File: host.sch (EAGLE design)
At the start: 106 parts, among them IC1 74LVC1T45GS,132, IC10 74LVC1T45GS,132, IC11 74LVC1T45GS,132, IC2 NCP187AMT120TAG, IC3 LD39200PU33R, IC4 74LVC1T45GS,132, IC5 74LVC1T45GS,132, IC6 74LVC1T45GS,132, IC7 74ALVC164245DGG:11, IC8 74ALVC164245DGG:11, IC9 74LVC1T45GS,132, Y1 DSC6001J

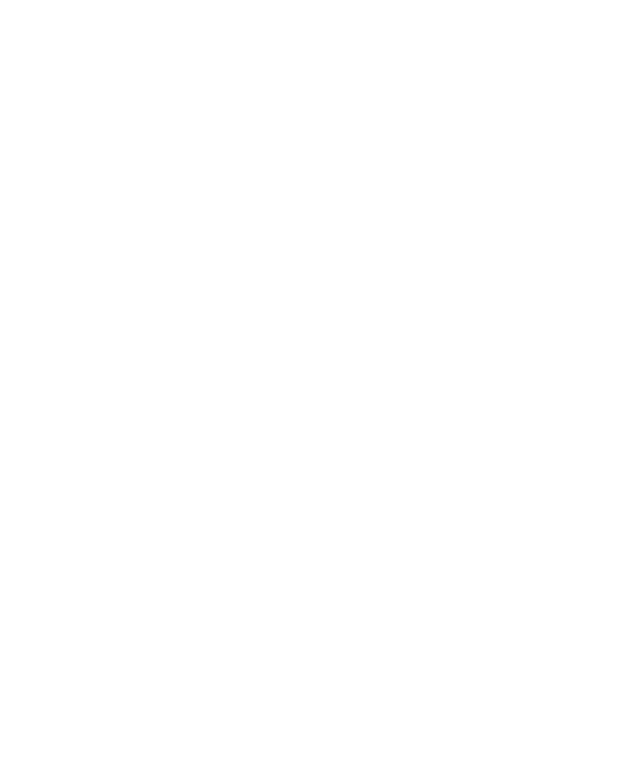
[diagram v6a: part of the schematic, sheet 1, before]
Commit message: Move to micro-HDMI for the interconnect cable
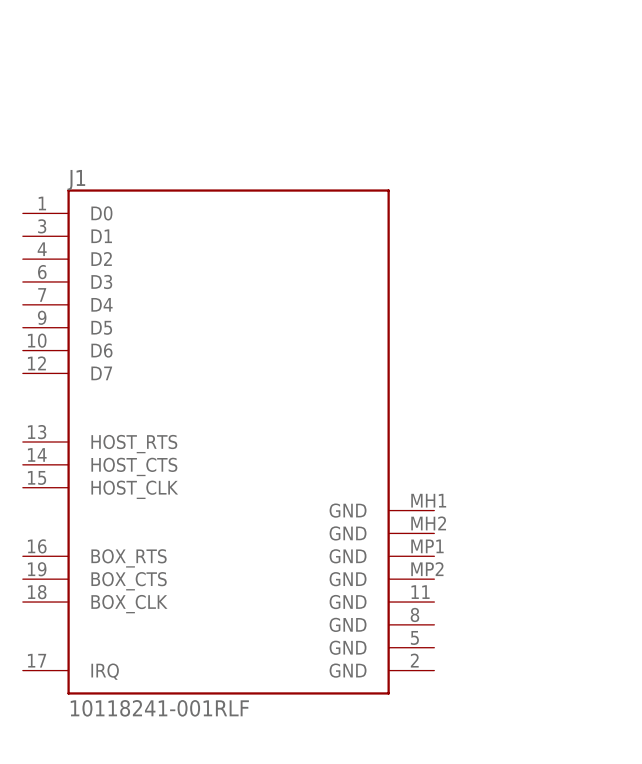
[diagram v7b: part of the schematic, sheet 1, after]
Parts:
- added J1: 10118241-001RLF, host:10118241-001RLF
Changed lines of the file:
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@@
 <attribute name="USE" value="CR0201-JW-103GLF"/>
 </part>
+<part name="J1" library="host" deviceset="10118241-001RLF" device=""/>
 </parts>
 <sheets>
@@
 <attribute name="VALUE" x="228.6" y="203.2" size="1.778" layer="96" rot="MR180"/>
 </instance>
+<instance part="J1" gate="G$1" x="142.24" y="142.24" smashed="yes">
+<attribute name="NAME" x="124.46" y="168.148" size="1.778" layer="95"/>
+<attribute name="VALUE" x="124.46" y="109.22" size="1.778" layer="96"/>
+</instance>
 </instances>

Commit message: Add in the debug headers
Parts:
- added DBG_CART: (no value), pinhead-2:PINHD-2X15_2.54
- added DBG_EXT: (no value), pinhead-2:PINHD-2X07_2.54
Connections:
- new net AUDIO: DBG_EXT.5, U$2.E5:AUDIO
- new net RSRVD: DBG_EXT.14, U$2.EA:RSRVD
- net !A8_CCTL!: now also DBG_CART.1
- net !A8_CLK!: now also DBG_CART.2
- net !A8_D1XX!: now also DBG_EXT.9
- net !A8_EXTSEL!: now also DBG_EXT.13
- net !A8_HALT!: now also DBG_EXT.10
- net !A8_IRQ!: now also DBG_EXT.12
- net !A8_MPD!: now also DBG_EXT.7
- net !A8_REF!: now also DBG_EXT.3
- net !A8_RESET!: now also DBG_EXT.11
- net !A8_S4!: now also DBG_CART.29
- net !A8_S5!: now also DBG_CART.7
- net +5V: now also DBG_CART.5, DBG_EXT.1
- net A8_A0: now also DBG_CART.21
- net A8_A1: now also DBG_CART.23
- net A8_A10: now also DBG_CART.6
- net A8_A11: now also DBG_CART.8
- net A8_A12: now also DBG_CART.14
- net A8_A13: now also DBG_EXT.8
- net A8_A14: now also DBG_EXT.6
- net A8_A15: now also DBG_EXT.4
- net A8_A2: now also DBG_CART.25
- net A8_A3: now also DBG_CART.27
- net A8_A4: now also DBG_CART.26
- net A8_A5: now also DBG_CART.24
- net A8_A6: now also DBG_CART.22
- net A8_A7: now also DBG_CART.20
- net A8_A8: now also DBG_CART.18
- net A8_A9: now also DBG_CART.16
- net A8_D0: now also DBG_CART.11
- net A8_D1: now also DBG_CART.13
- net A8_D2: now also DBG_CART.15
- net A8_D3: now also DBG_CART.12
- net A8_D4: now also DBG_CART.19
- net A8_D5: now also DBG_CART.17
- net A8_D6: now also DBG_CART.9
- net A8_D7: now also DBG_CART.10
- net A8_R/!W!: now also DBG_CART.4
- net A8_RD4: now also DBG_CART.30
- net A8_RD5: now also DBG_CART.3
- net GND: now also DBG_CART.28, DBG_EXT.2
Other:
- moved on the sheet: C43, C44, C45, C46, C47, C48, C49, C50, CBSEL0, CBSEL1, J1, R10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
